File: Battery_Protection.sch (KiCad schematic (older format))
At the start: 101 parts, among them J10 JST 2P-1.0, J11 JST 2P-1.0, J4 JST 2P-1.0, J5 JST 2P-1.0, J6 JST 2P-1.0, J7 JST 2P-1.0, J8 JST 2P-1.0, J9 JST 2P-1.0, Q2 2n7002K, Q4 AO4468, Q6 AO4468, Q7 2n7002K, SW1 SW_Push, SW2 SW_Push, U2 BQ294706DSGR, U3 ITV4030, U4 BQ40Z50

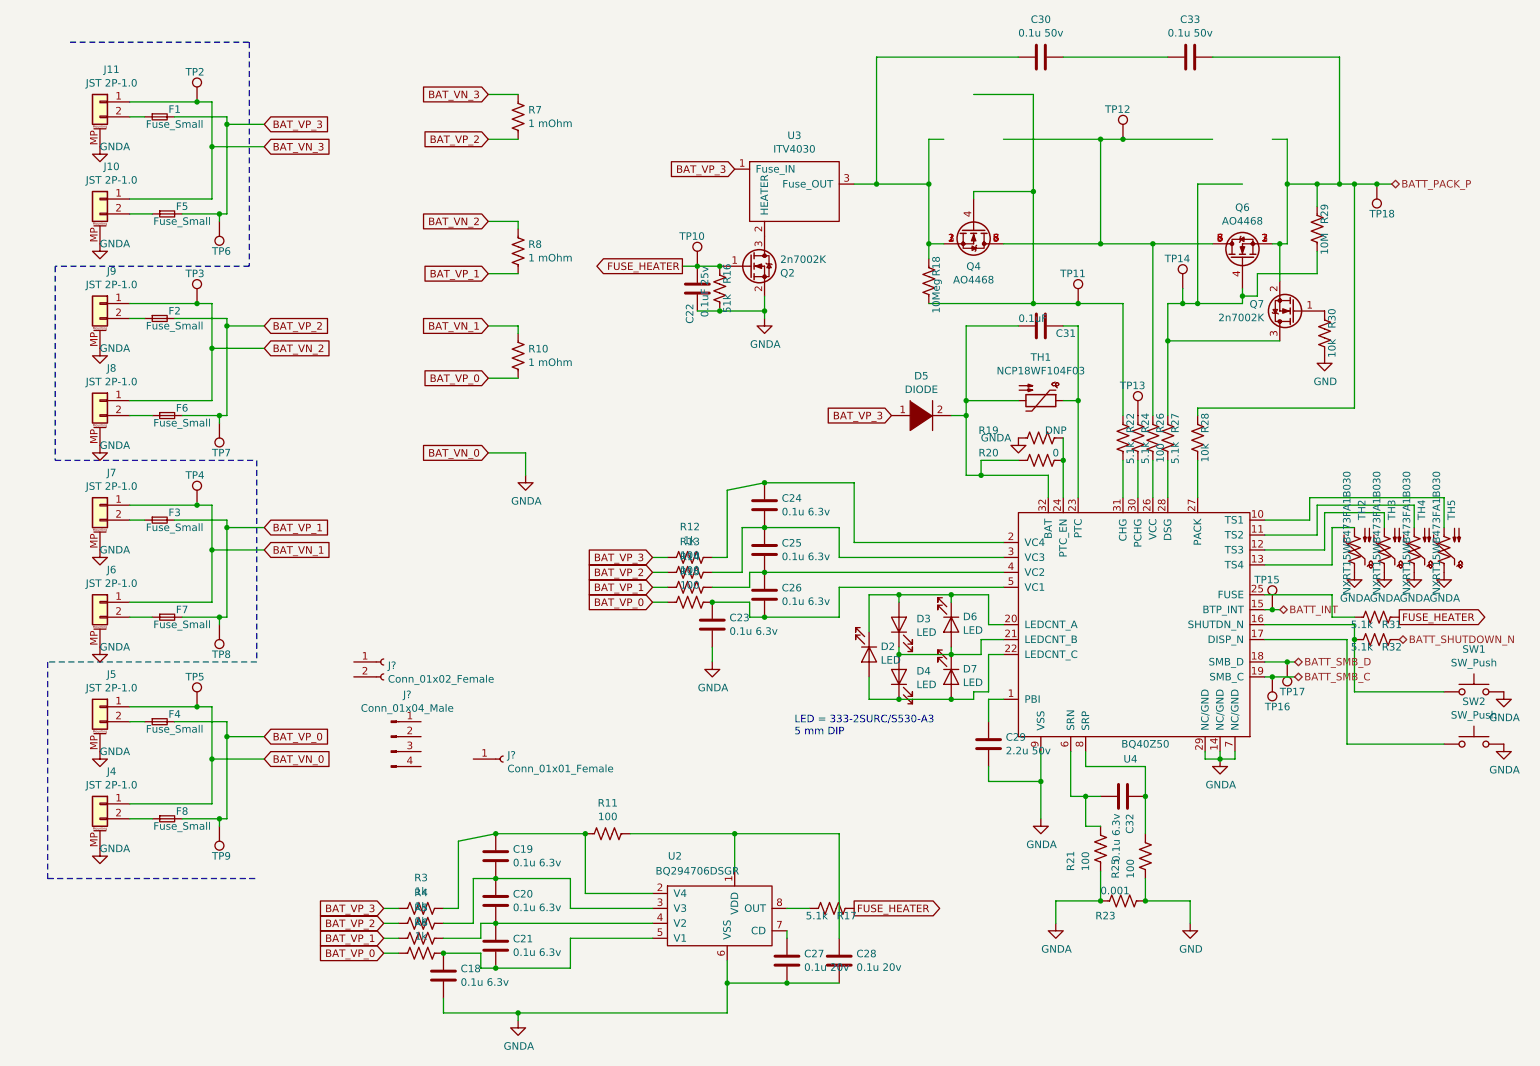
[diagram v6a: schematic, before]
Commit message: Switching over to jlpcb
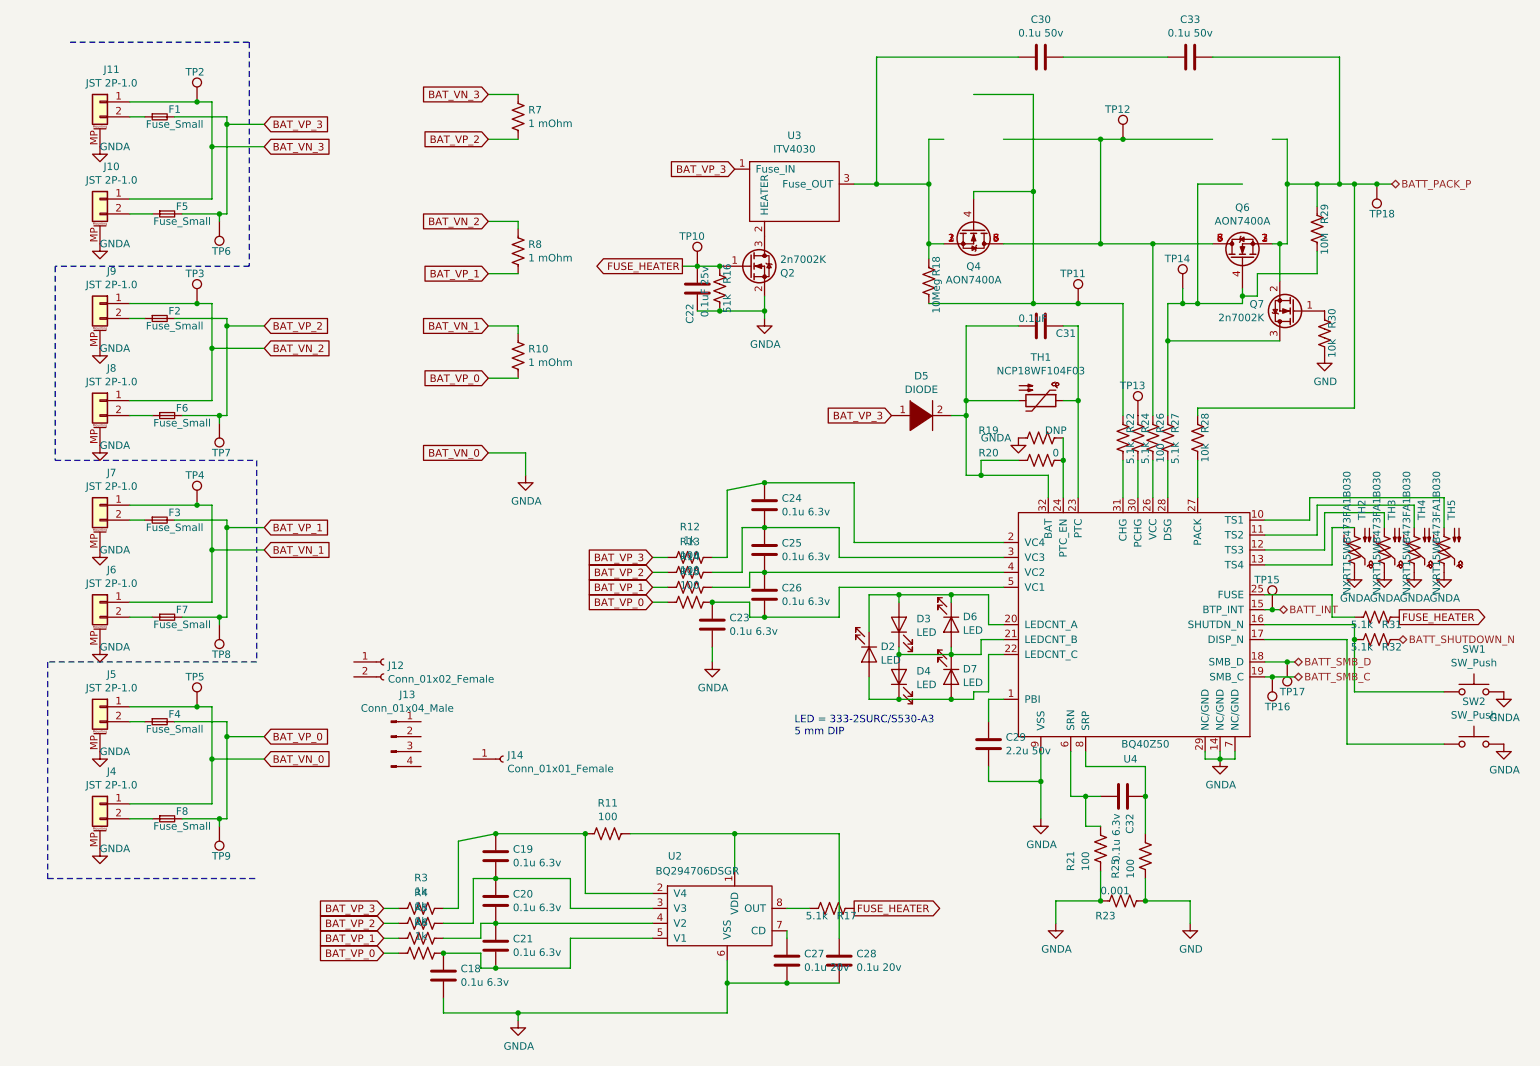
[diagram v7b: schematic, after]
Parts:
- C18, C19, C20, C21, C23, C24, C25, C26, C31, C32: footprint Capacitor_SMD:C_0201_0603Metric -> lc_lib:0402_C
- C22, C27, C28: footprint Capacitor_SMD:C_0402_1005Metric -> lc_lib:0402_C
- C29: footprint Capacitor_SMD:C_0603_1608Metric -> lc_lib:0805_C
- C30, C33: footprint Capacitor_SMD:C_0603_1608Metric -> lc_lib:0402_C
- D5: footprint Diode_SMD:D_0201_0603Metric -> lc_lib:SOD-123
- F1, F2, F3, F4, F5, F6, F7, F8: footprint Fuse:Fuse_1206_3216Metric_Pad1.42x1.75mm_HandSolder -> lc_lib:1206
- Q4: value AO4468 -> AON7400A; footprint SmartBattery:SOIC-8_Alpha_Omega -> lc_lib:QFN-8_3X3X065P; LCSC (none) -> C85734; SKU AO4468 -> (none)
- Q6: value AO4468 -> AON7400A; footprint SmartBattery:SOIC-8_Alpha_Omega -> lc_lib:QFN-8_3X3X065P; SKU AO4468 -> AON7400A
- R10, R7, R8: footprint Resistor_SMD:R_1206_3216Metric -> lc_lib:1206_R
- R11, R12, R13, R14, R15, R16, R17, R18, R19, R20, R21, R22, R24, R25, R26, R27, R28, R29, R3, R30, R31, R32, R4, R5, R6: footprint Resistor_SMD:R_0201_0603Metric -> lc_lib:0402_R
- SW1, SW2: footprint Button_Switch_SMD:SW_Push_1P1T_NO_6x6mm_H9.5mm -> lc_lib:0402_R
- U2: LCSC (none) -> C216211; SKU BQ294706DSGR -> (none)
- gave numbers to parts that had none: 3

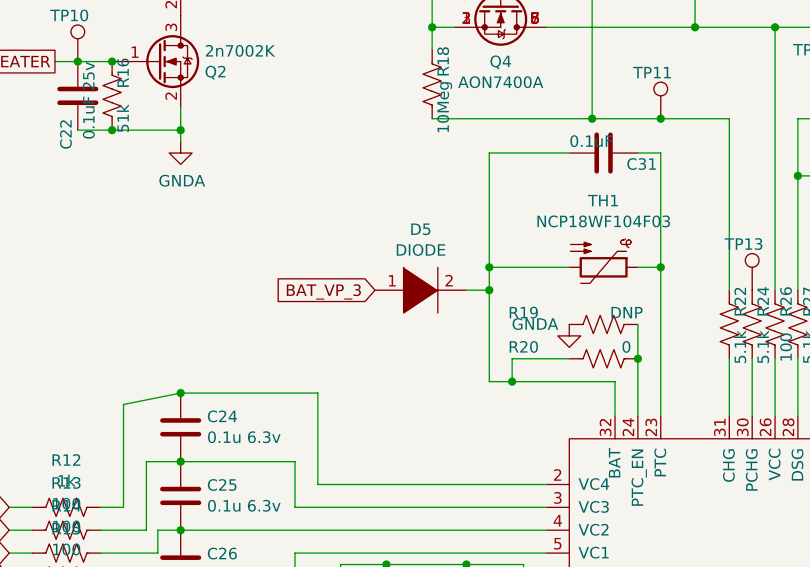
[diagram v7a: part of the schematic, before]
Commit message: Replaced old charger to support JLC assembly. Very close now!
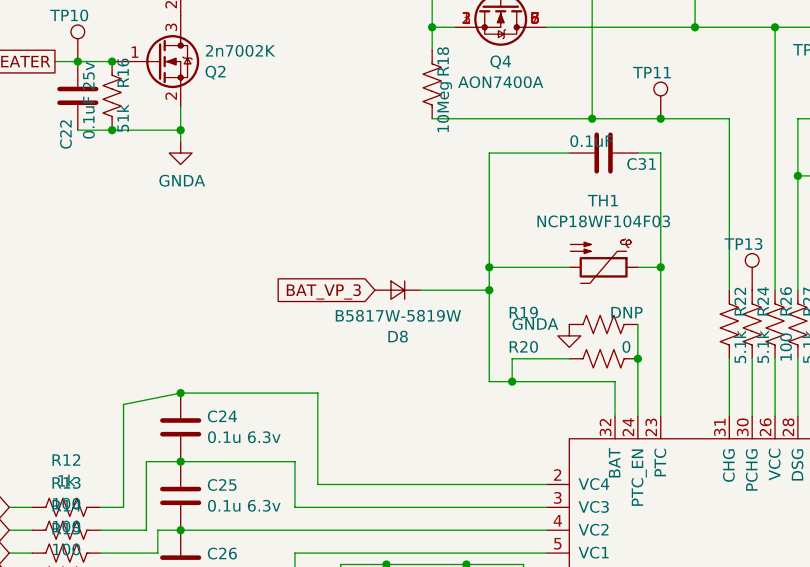
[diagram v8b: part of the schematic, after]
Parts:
- removed D5: DIODE, lc_lib:SOD-123, symbol pspice:DIODE
- added D8: B5817W-5819W, lc_lib:SOD-123, symbol Device:D_Small
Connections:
- net BAT_VP_3: now also D8.2 (A)
- net at C31.2, R20.2, TH1.2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: now also D8.1 (K)
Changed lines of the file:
@@
 Wire Wire Line
 	5550 6500 5700 6500
-$Comp
-L pspice:DIODE D5
-U 1 1 6036B8C2
-P 6450 3200
-F 0 "D5" H 6450 3465 50  0000 C CNN
-F 1 "DIODE" H 6450 3374 50  0000 C CNN
-F 2 "lc_lib:SOD-123" H 6450 3200 50  0001 C CNN
-F 3 "~" H 6450 3200 50  0001 C CNN
-	1    6450 3200
-	1    0    0    -1
-$EndComp
-Wire Wire Line
-	6650 3200 6750 3200
 Connection ~ 6750 3200
 Wire Wire Line
@@
 	1    0    0    -1
 $EndComp
+$Comp
+L Device:D_Small D?
+U 1 1 5FF3FC67
+P 6350 3200
+AR Path="/5FD99B08/5FF3FC67" Ref="D?"  Part="1"
+AR Path="/5FD15753/5FF3FC67" Ref="D8"  Part="1"
+F 0 "D8" H 6350 3405 50  0000 C CNN
+F 1 "B5817W-5819W" H 6350 3314 50  0000 C CNN
+F 2 "lc_lib:SOD-123" V 6350 3200 50  0001 C CNN
+F 3 "~" V 6350 3200 50  0001 C CNN
+F 4 "304040005" H 6350 3200 50  0001 C CNN "lcsc"
+	1    6350 3200
+	-1   0    0    1
+$EndComp
+Wire Wire Line
+	6450 3200 6750 3200
 $EndSCHEMATC
